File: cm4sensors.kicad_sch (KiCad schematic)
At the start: 22 parts, among them J3 TSM-102-01-L-SV, J4 TSM-102-01-L-SV, U7 MCP9808T-E_MC, U8 ADS7142IRUGR, U9 MCP9808T-E_MC

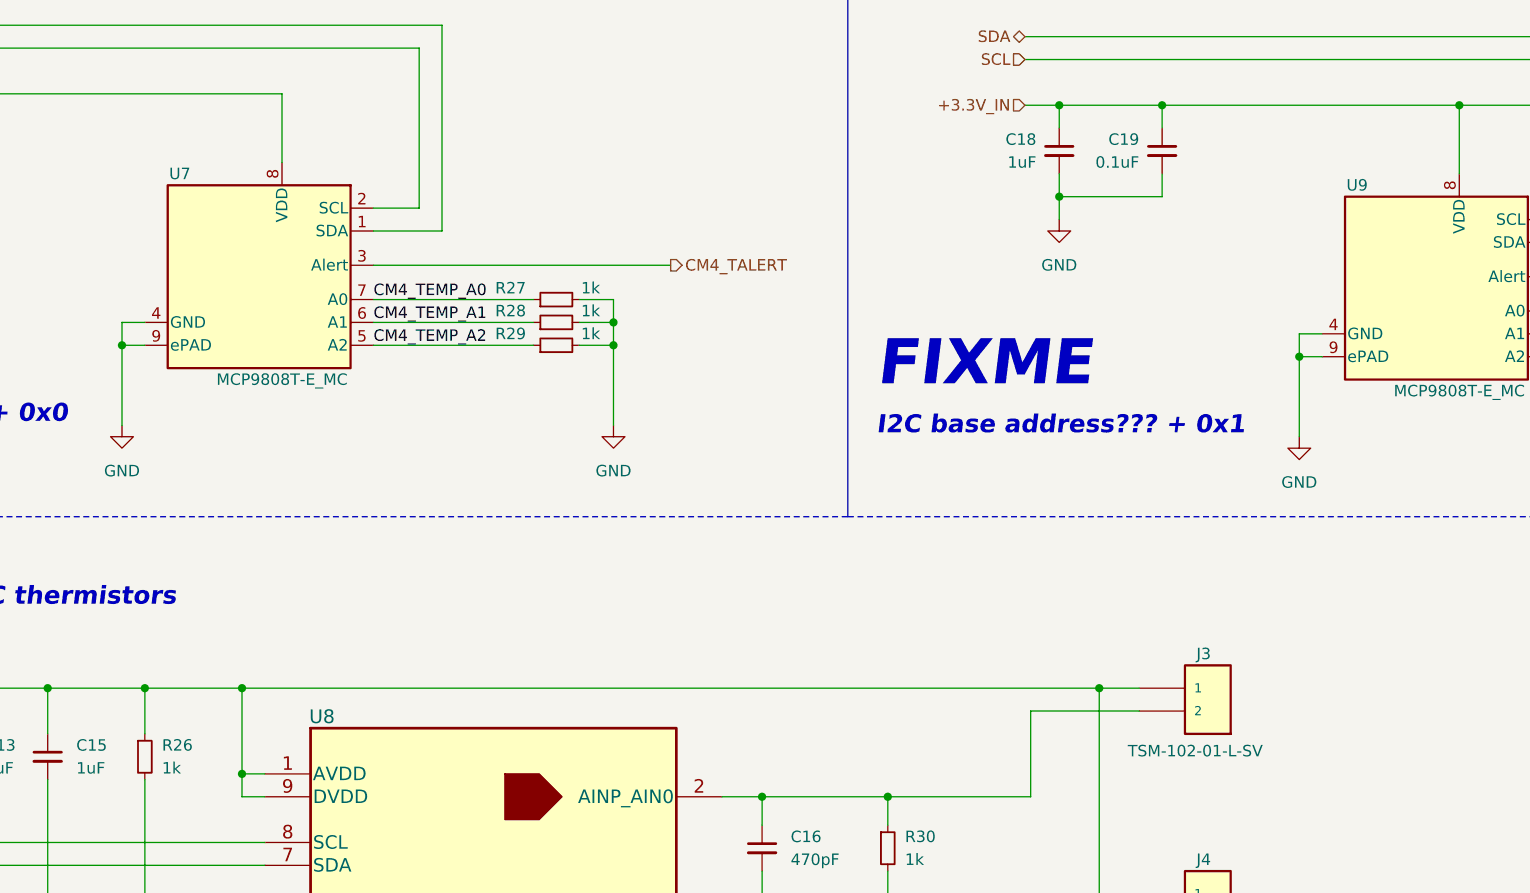
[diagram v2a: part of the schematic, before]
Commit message: added ti buffer lib
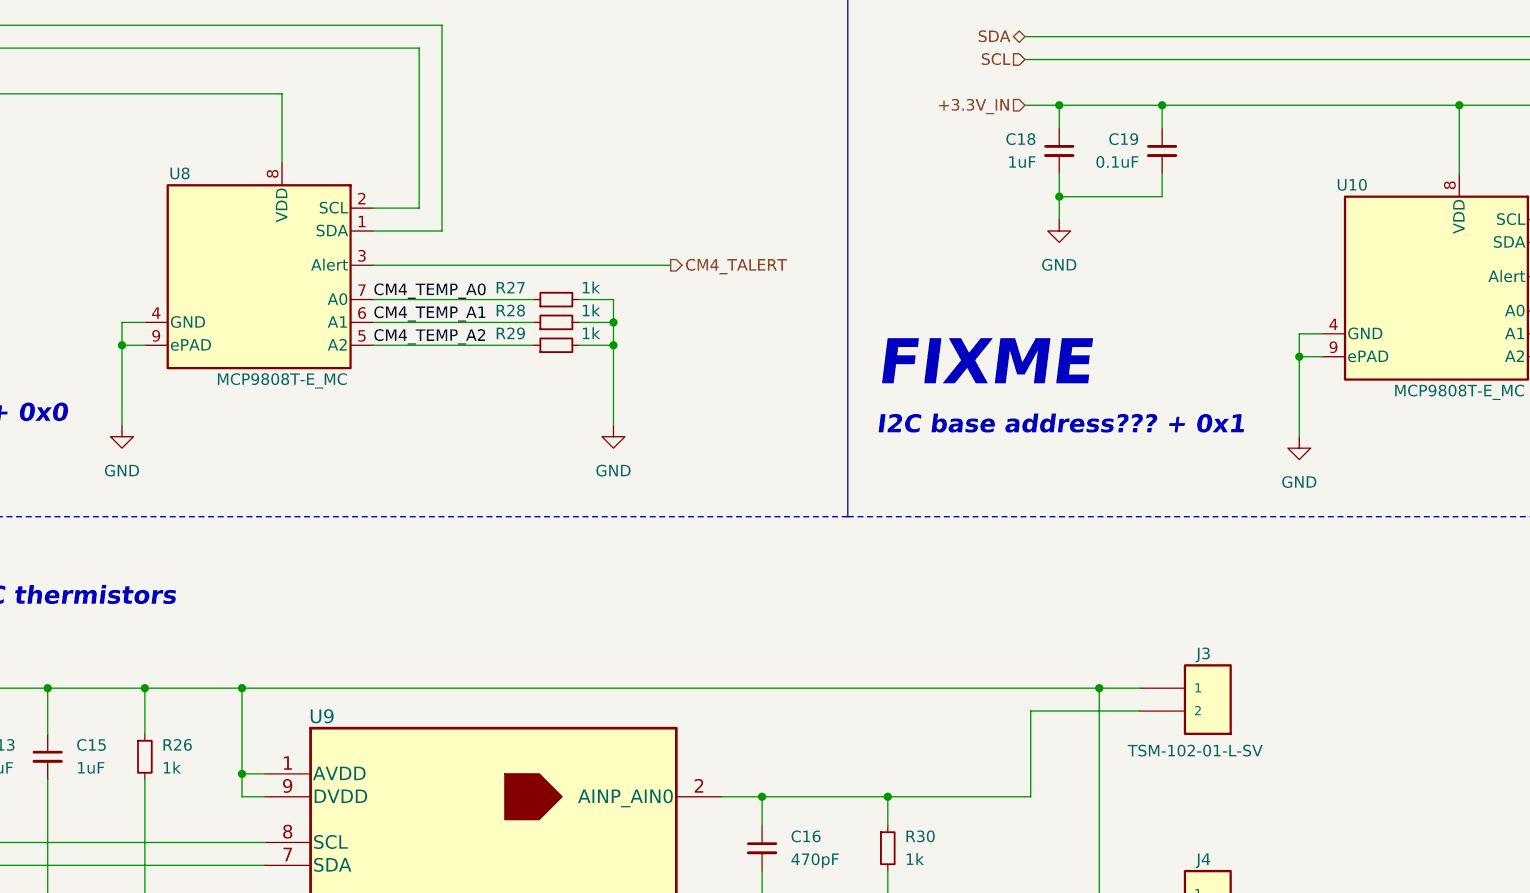
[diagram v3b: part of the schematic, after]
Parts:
- renumbered U9 to U10, U7 to U8, U8 to U9
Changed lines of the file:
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@@
   (symbol (lib_id "Sensor_I2C_Microchip:MCP9808T-E_MC") (at 215.265 85.09 0) (mirror y) (unit 1)
     (in_bom yes) (on_board yes)
-    (property "Reference" "U9" (id 0) (at 205.105 73.66 0)
+    (property "Reference" "U10" (id 0) (at 205.105 73.66 0)
       (effects (font (size 1.27 1.27)) (justify left))
     )
@@
   (symbol (lib_id "power:GND") (at 121.285 100.33 0) (unit 1)
     (in_bom yes) (on_board yes) (fields_autoplaced)
-    (property "Reference" "#PWR024" (id 0) (at 121.285 106.68 0)
+    (property "Reference" "#PWR026" (id 0) (at 121.285 106.68 0)
       (effects (font (size 1.27 1.27)) hide)
     )
@@
   (symbol (lib_id "power:GND") (at 197.485 101.6 0) (mirror y) (unit 1)
     (in_bom yes) (on_board yes)
-    (property "Reference" "#PWR027" (id 0) (at 197.485 107.95 0)
+    (property "Reference" "#PWR029" (id 0) (at 197.485 107.95 0)
       (effects (font (size 1.27 1.27)) hide)
     )
@@
   (symbol (lib_name "MCP9808T-E_MC_1") (lib_id "Sensor_I2C_Microchip:MCP9808T-E_MC") (at 84.455 83.82 0) (mirror y) (unit 1)
     (in_bom yes) (on_board yes)
-    (property "Reference" "U7" (id 0) (at 74.295 72.39 0)
+    (property "Reference" "U8" (id 0) (at 74.295 72.39 0)
       (effects (font (size 1.27 1.27)) (justify left))
     )
@@
   (symbol (lib_id "Analog_ADC_TI:ADS7142IRUGR") (at 107.95 149.225 0) (unit 1)
     (in_bom yes) (on_board yes)
-    (property "Reference" "U8" (id 0) (at 88.9 132.715 0)
+    (property "Reference" "U9" (id 0) (at 88.9 132.715 0)
       (effects (font (size 1.524 1.524)))
     )
@@
   (symbol (lib_id "power:GND") (at 40.005 76.2 0) (mirror y) (unit 1)
     (in_bom yes) (on_board yes)
-    (property "Reference" "#PWR021" (id 0) (at 40.005 82.55 0)
+    (property "Reference" "#PWR023" (id 0) (at 40.005 82.55 0)
       (effects (font (size 1.27 1.27)) hide)
     )
@@
   (symbol (lib_id "power:GND") (at 170.815 77.47 0) (mirror y) (unit 1)
     (in_bom yes) (on_board yes)
-    (property "Reference" "#PWR026" (id 0) (at 170.815 83.82 0)
+    (property "Reference" "#PWR028" (id 0) (at 170.815 83.82 0)
       (effects (font (size 1.27 1.27)) hide)
     )
@@
   (symbol (lib_id "power:GND") (at 252.095 101.6 0) (mirror y) (unit 1)
     (in_bom yes) (on_board yes)
-    (property "Reference" "#PWR028" (id 0) (at 252.095 107.95 0)
+    (property "Reference" "#PWR030" (id 0) (at 252.095 107.95 0)
       (effects (font (size 1.27 1.27)) hide)
     )
@@
   (symbol (lib_id "power:GND") (at 164.465 177.165 0) (unit 1)
     (in_bom yes) (on_board yes) (fields_autoplaced)
-    (property "Reference" "#PWR025" (id 0) (at 164.465 183.515 0)
+    (property "Reference" "#PWR027" (id 0) (at 164.465 183.515 0)
       (effects (font (size 1.27 1.27)) hide)
     )
@@
   (symbol (lib_id "power:GND") (at 48.26 177.165 0) (unit 1)
     (in_bom yes) (on_board yes) (fields_autoplaced)
-    (property "Reference" "#PWR022" (id 0) (at 48.26 183.515 0)
+    (property "Reference" "#PWR024" (id 0) (at 48.26 183.515 0)
       (effects (font (size 1.27 1.27)) hide)
     )
@@
   (symbol (lib_id "power:GND") (at 66.675 100.33 0) (unit 1)
     (in_bom yes) (on_board yes) (fields_autoplaced)
-    (property "Reference" "#PWR023" (id 0) (at 66.675 106.68 0)
-      (effects (font (size 1.27 1.27)) hide)
-    )
+    (property "Reference" "#PWR025" (id 0) (at 66.675 106.68 0)
+      (effects (font (size 1.27 1.27)) hide)
+    )

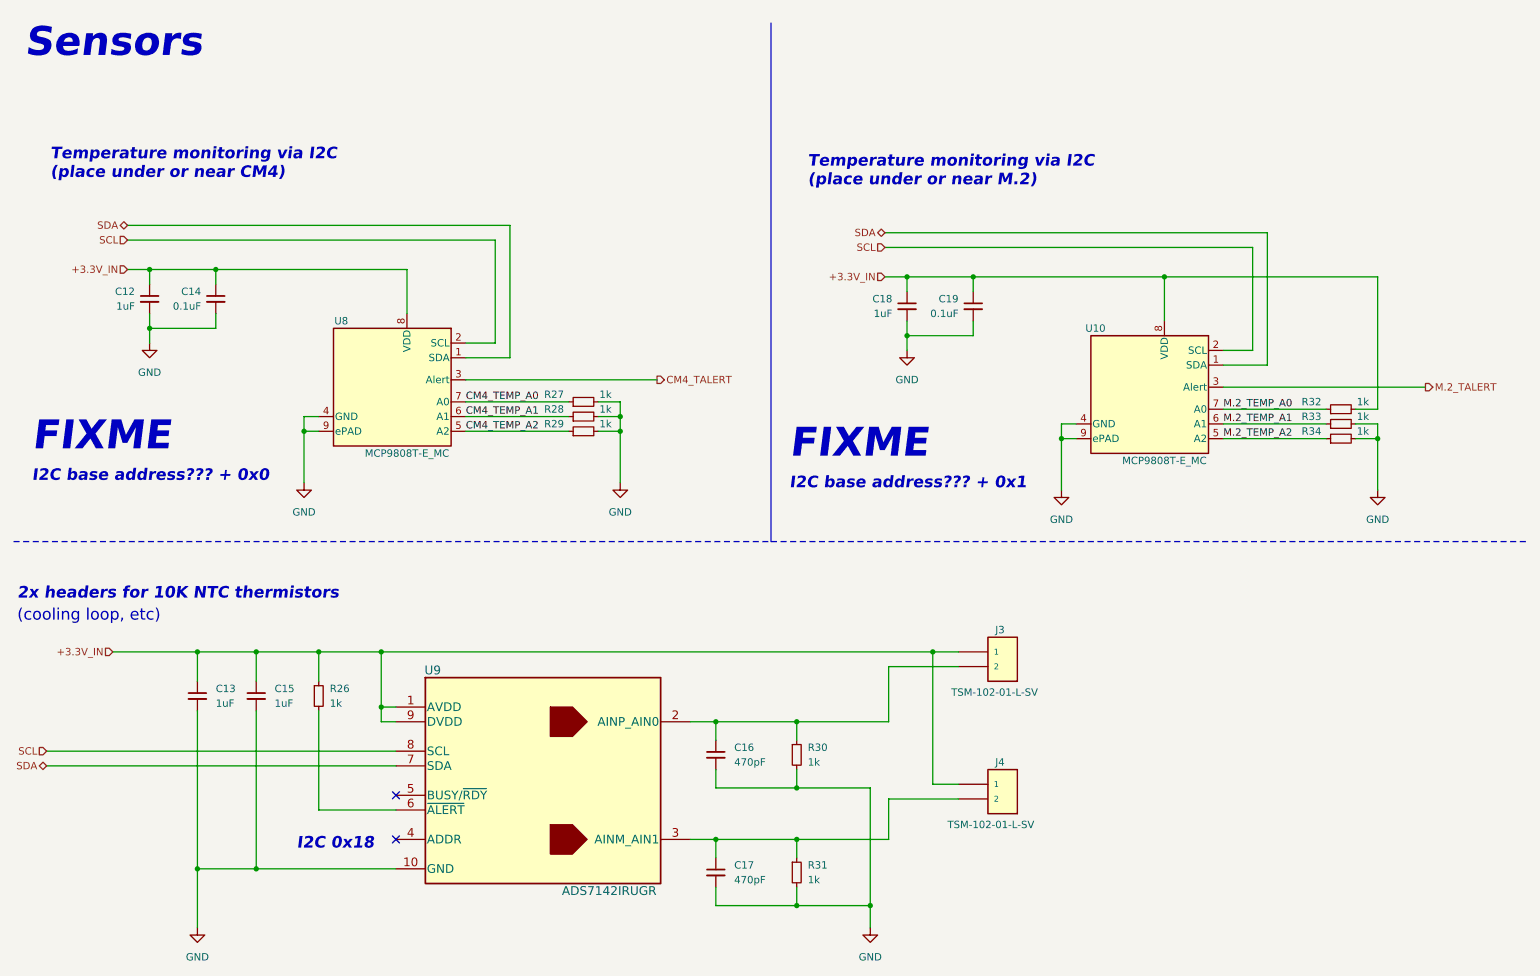
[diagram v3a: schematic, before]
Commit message: initial integration of i2c arbiter
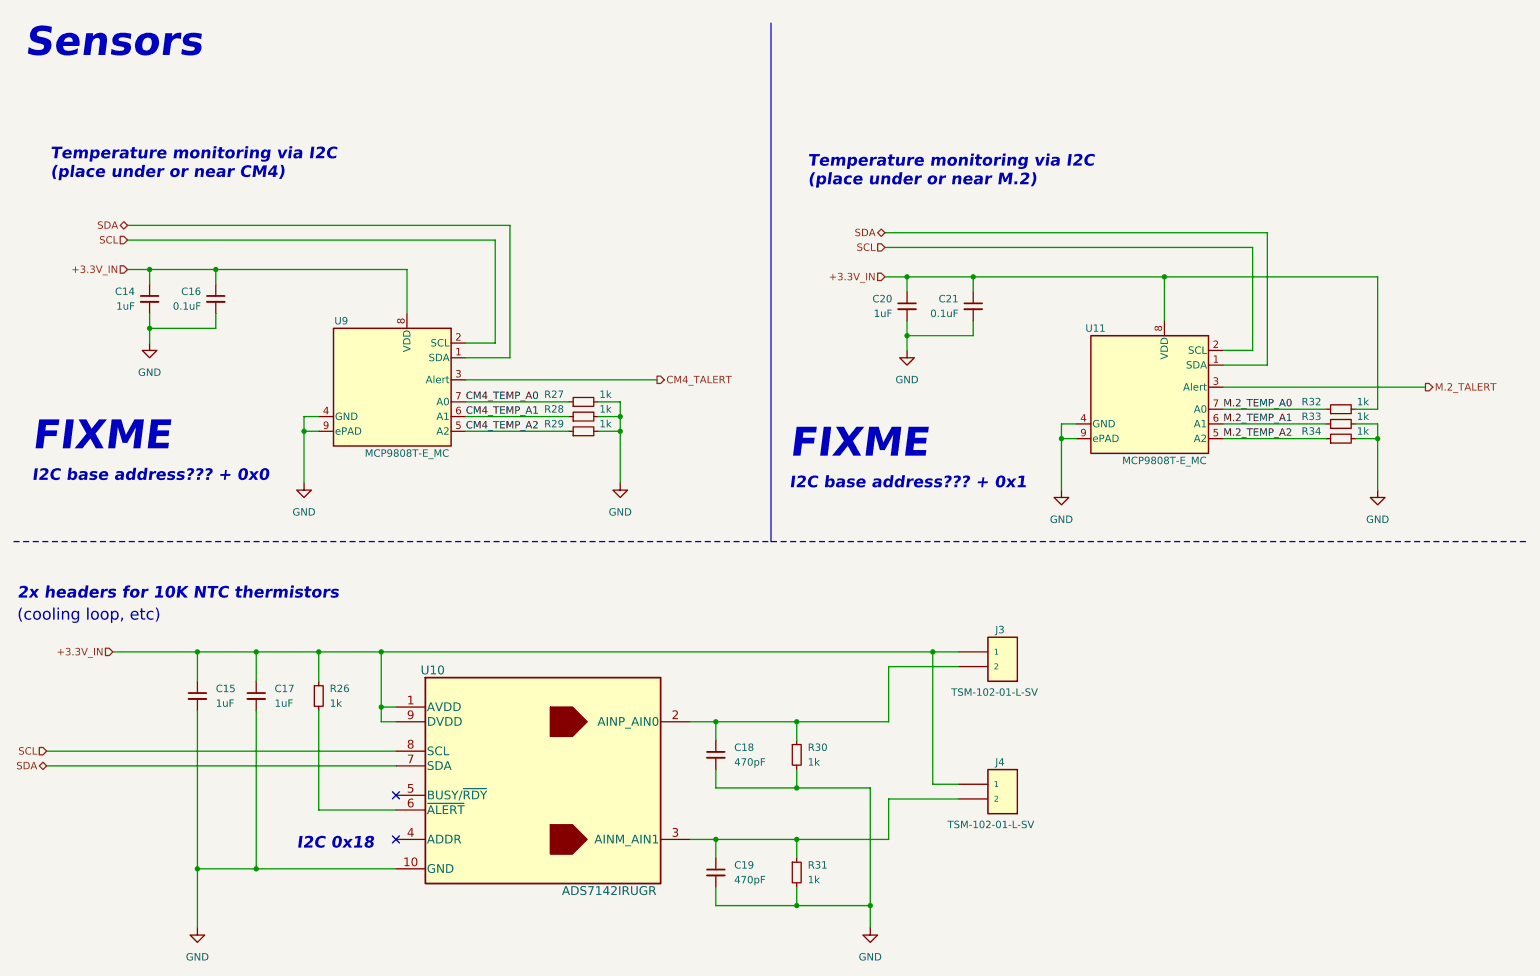
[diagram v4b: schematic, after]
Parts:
- renumbered C12 to C14, C13 to C15, C14 to C16, C15 to C17, C16 to C18, C17 to C19, C18 to C20, C19 to C21, U9 to U10, U10 to U11, U8 to U9
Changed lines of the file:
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@@
   (symbol (lib_id "Device:C_Small") (at 137.795 147.32 0) (unit 1)
     (in_bom yes) (on_board yes) (fields_autoplaced)
-    (property "Reference" "C16" (id 0) (at 140.97 146.0562 0)
+    (property "Reference" "C18" (id 0) (at 140.97 146.0562 0)
       (effects (font (size 1.27 1.27)) (justify left))
     )
@@
   (symbol (lib_id "Sensor_I2C_Microchip:MCP9808T-E_MC") (at 215.265 85.09 0) (mirror y) (unit 1)
     (in_bom yes) (on_board yes)
-    (property "Reference" "U10" (id 0) (at 205.105 73.66 0)
+    (property "Reference" "U11" (id 0) (at 205.105 73.66 0)
       (effects (font (size 1.27 1.27)) (justify left))
     )
@@
   (symbol (lib_id "power:GND") (at 121.285 100.33 0) (unit 1)
     (in_bom yes) (on_board yes) (fields_autoplaced)
-    (property "Reference" "#PWR026" (id 0) (at 121.285 106.68 0)
+    (property "Reference" "#PWR027" (id 0) (at 121.285 106.68 0)
       (effects (font (size 1.27 1.27)) hide)
     )
@@
   (symbol (lib_id "power:GND") (at 197.485 101.6 0) (mirror y) (unit 1)
     (in_bom yes) (on_board yes)
-    (property "Reference" "#PWR029" (id 0) (at 197.485 107.95 0)
+    (property "Reference" "#PWR030" (id 0) (at 197.485 107.95 0)
       (effects (font (size 1.27 1.27)) hide)
     )
@@
   (symbol (lib_id "Device:C_Small") (at 51.435 68.58 0) (mirror y) (unit 1)
     (in_bom yes) (on_board yes) (fields_autoplaced)
-    (property "Reference" "C14" (id 0) (at 48.895 67.31 0)
+    (property "Reference" "C16" (id 0) (at 48.895 67.31 0)
       (effects (font (size 1.27 1.27)) (justify left))
     )
@@
   (symbol (lib_name "MCP9808T-E_MC_1") (lib_id "Sensor_I2C_Microchip:MCP9808T-E_MC") (at 84.455 83.82 0) (mirror y) (unit 1)
     (in_bom yes) (on_board yes)
-    (property "Reference" "U8" (id 0) (at 74.295 72.39 0)
+    (property "Reference" "U9" (id 0) (at 74.295 72.39 0)
       (effects (font (size 1.27 1.27)) (justify left))
     )
@@
   (symbol (lib_id "Analog_ADC_TI:ADS7142IRUGR") (at 107.95 149.225 0) (unit 1)
     (in_bom yes) (on_board yes)
-    (property "Reference" "U9" (id 0) (at 88.9 132.715 0)
+    (property "Reference" "U10" (id 0) (at 88.9 132.715 0)
       (effects (font (size 1.524 1.524)))
     )
@@
   (symbol (lib_id "Device:C_Small") (at 182.245 69.85 0) (mirror y) (unit 1)
     (in_bom yes) (on_board yes) (fields_autoplaced)
-    (property "Reference" "C19" (id 0) (at 179.705 68.58 0)
+    (property "Reference" "C21" (id 0) (at 179.705 68.58 0)
       (effects (font (size 1.27 1.27)) (justify left))
     )
@@
   (symbol (lib_id "power:GND") (at 40.005 76.2 0) (mirror y) (unit 1)
     (in_bom yes) (on_board yes)
-    (property "Reference" "#PWR023" (id 0) (at 40.005 82.55 0)
+    (property "Reference" "#PWR024" (id 0) (at 40.005 82.55 0)
       (effects (font (size 1.27 1.27)) hide)
     )
@@
   (symbol (lib_id "power:GND") (at 170.815 77.47 0) (mirror y) (unit 1)
     (in_bom yes) (on_board yes)
-    (property "Reference" "#PWR028" (id 0) (at 170.815 83.82 0)
+    (property "Reference" "#PWR029" (id 0) (at 170.815 83.82 0)
       (effects (font (size 1.27 1.27)) hide)
     )
@@
   (symbol (lib_id "power:GND") (at 252.095 101.6 0) (mirror y) (unit 1)
     (in_bom yes) (on_board yes)
-    (property "Reference" "#PWR030" (id 0) (at 252.095 107.95 0)
+    (property "Reference" "#PWR031" (id 0) (at 252.095 107.95 0)
       (effects (font (size 1.27 1.27)) hide)
     )
@@
   (symbol (lib_id "Device:C_Small") (at 137.795 167.64 0) (unit 1)
     (in_bom yes) (on_board yes) (fields_autoplaced)
-    (property "Reference" "C17" (id 0) (at 140.97 166.3762 0)
+    (property "Reference" "C19" (id 0) (at 140.97 166.3762 0)
       (effects (font (size 1.27 1.27)) (justify left))
     )
@@
   (symbol (lib_id "Device:C_Small") (at 48.26 137.16 0) (unit 1)
     (in_bom yes) (on_board yes) (fields_autoplaced)
-    (property "Reference" "C13" (id 0) (at 51.435 135.8962 0)
+    (property "Reference" "C15" (id 0) (at 51.435 135.8962 0)
       (effects (font (size 1.27 1.27)) (justify left))
     )
@@
   (symbol (lib_id "power:GND") (at 164.465 177.165 0) (unit 1)
     (in_bom yes) (on_board yes) (fields_autoplaced)
-    (property "Reference" "#PWR027" (id 0) (at 164.465 183.515 0)
+    (property "Reference" "#PWR028" (id 0) (at 164.465 183.515 0)
       (effects (font (size 1.27 1.27)) hide)
     )
@@
   (symbol (lib_id "power:GND") (at 48.26 177.165 0) (unit 1)
     (in_bom yes) (on_board yes) (fields_autoplaced)
-    (property "Reference" "#PWR024" (id 0) (at 48.26 183.515 0)
+    (property "Reference" "#PWR025" (id 0) (at 48.26 183.515 0)
       (effects (font (size 1.27 1.27)) hide)
     )
@@
   (symbol (lib_id "Device:C_Small") (at 40.005 68.58 0) (mirror y) (unit 1)
     (in_bom yes) (on_board yes) (fields_autoplaced)
-    (property "Reference" "C12" (id 0) (at 37.465 67.31 0)
+    (property "Reference" "C14" (id 0) (at 37.465 67.31 0)
       (effects (font (size 1.27 1.27)) (justify left))
     )
@@
   (symbol (lib_id "Device:C_Small") (at 170.815 69.85 0) (mirror y) (unit 1)
     (in_bom yes) (on_board yes) (fields_autoplaced)
-    (property "Reference" "C18" (id 0) (at 168.275 68.58 0)
+    (property "Reference" "C20" (id 0) (at 168.275 68.58 0)
       (effects (font (size 1.27 1.27)) (justify left))
     )
@@
   (symbol (lib_id "Device:C_Small") (at 58.42 137.16 0) (unit 1)
     (in_bom yes) (on_board yes) (fields_autoplaced)
-    (property "Reference" "C15" (id 0) (at 61.595 135.8962 0)
+    (property "Reference" "C17" (id 0) (at 61.595 135.8962 0)
       (effects (font (size 1.27 1.27)) (justify left))
     )
@@
   (symbol (lib_id "power:GND") (at 66.675 100.33 0) (unit 1)
     (in_bom yes) (on_board yes) (fields_autoplaced)
-    (property "Reference" "#PWR025" (id 0) (at 66.675 106.68 0)
-      (effects (font (size 1.27 1.27)) hide)
-    )
+    (property "Reference" "#PWR026" (id 0) (at 66.675 106.68 0)
+      (effects (font (size 1.27 1.27)) hide)
+    )
